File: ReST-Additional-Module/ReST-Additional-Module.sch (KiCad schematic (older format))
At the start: 15 parts, among them P1 02X10-MALE, P3 02-SCREW-TERM, P4 01X02-MALE, P5 02-SCREW-TERM, Q1 Q_BSH105

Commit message: Added Additional Module
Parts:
- removed C1: 10uF, ok-smd-generic:1206, symbol C
- removed P1: 02X10-MALE, Pin_Headers:Pin_Header_Angled_2x10, symbol CONN_02X10
- removed P4: 01X02-MALE, Pin_Headers:Pin_Header_Straight_1x02, symbol CONN_01X02
- removed P?: CONN_02X06, symbol CONN_02X06
- removed Q?: Q_NMOS_GSD, symbol Q_NMOS_GSD
- removed R1: 4.7K, ok-smd-generic:1206, symbol R
- added P1: CONN_02X06, Pin_Headers:Pin_Header_Angled_2x06, symbol CONN_02X06
- added Q2: Q_AOT240L, TO_SOT_Packages_THT:TO-220_Neutral123_Vertical_LargePads, symbol Q_NMOS_GDS
- P2: renamed from P5; footprint 5mm-pitch-terminal:mkds_1,5-2 -> Pin_Headers:Pin_Header_Straight_1x02
- P3: footprint 2:mpt_0,5%2f2-2,54 -> 5mm-pitch-terminal:mkds_1,5-2
- renumbered R2 to R1, R3 to R2, R4 to R3, R5 to R4
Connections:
- net labels added: PWM-ADD
- net labels removed: PWM-HEATER, T1
- wire segments 84 -> 40
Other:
- note removed: "Heater Thermistor"
- moved on the sheet: D1, D2, P2, Q1, R1, R2, R3, R4

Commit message: Saving
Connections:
- net +12V: now also P1.10 (P10), P1.12 (P12); no longer P1.2 (P2), P1.4 (P4)
- net +3V3: now also P1.4 (P4); no longer P1.10 (P10)
- net +5V: now also P1.1 (P1); no longer P1.9 (P9)
- net GND: now also P1.9 (P9); no longer P1.1 (P1), P1.3 (P3)
- net PWM-ADD: now also P1.3 (P3); no longer P1.12 (P12)
- no-connect marks 0 -> 1
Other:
- moved on the sheet: P1
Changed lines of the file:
@@
 L +5V #PWR02
 U 1 1 56A6A1BB
-P 2950 2900
-F 0 "#PWR02" H 2950 2750 50  0001 C CNN
-F 1 "+5V" H 2950 3040 50  0000 C CNN
-F 2 "" H 2950 2900 50  0000 C CNN
-F 3 "" H 2950 2900 50  0000 C CNN
-	1    2950 2900
-	0    -1   -1   0
+P 3050 3100
+F 0 "#PWR02" H 3050 2950 50  0001 C CNN
+F 1 "+5V" H 3050 3240 50  0000 C CNN
+F 2 "" H 3050 3100 50  0000 C CNN
+F 3 "" H 3050 3100 50  0000 C CNN
+	1    3050 3100
+	-1   0    0    1
 $EndComp
 $Comp
 L +3V3 #PWR03
 U 1 1 56A6A1DD
-P 3800 2900
-F 0 "#PWR03" H 3800 2750 50  0001 C CNN
-F 1 "+3V3" H 3800 3040 50  0000 C CNN
-F 2 "" H 3800 2900 50  0000 C CNN
-F 3 "" H 3800 2900 50  0000 C CNN
-	1    3800 2900
-	1    0    0    -1
+P 3750 2900
+F 0 "#PWR03" H 3750 2750 50  0001 C CNN
+F 1 "+3V3" H 3750 3040 50  0000 C CNN
+F 2 "" H 3750 2900 50  0000 C CNN
+F 3 "" H 3750 2900 50  0000 C CNN
+	1    3750 2900
+	0    1    1    0
 $EndComp
 $Comp
 L GND #PWR04
-U 1 1 56A6A1FF
-P 2950 3100
-F 0 "#PWR04" H 2950 2850 50  0001 C CNN
-F 1 "GND" H 2950 2950 50  0000 C CNN
-F 2 "" H 2950 3100 50  0000 C CNN
-F 3 "" H 2950 3100 50  0000 C CNN
-	1    2950 3100
-	1    0    0    -1
-$EndComp
-$Comp
-L GND #PWR05
 U 1 1 56A6B6EF
 P 6850 3850
-F 0 "#PWR05" H 6850 3600 50  0001 C CNN
+F 0 "#PWR04" H 6850 3600 50  0001 C CNN
 F 1 "GND" H 6850 3700 50  0000 C CNN
 F 2 "" H 6850 3850 50  0000 C CNN
@@
 $EndComp
 $Comp
-L +3V3 #PWR06
+L +3V3 #PWR05
 U 1 1 56A6D2B8
 P 5150 3250
-F 0 "#PWR06" H 5150 3100 50  0001 C CNN
+F 0 "#PWR05" H 5150 3100 50  0001 C CNN
 F 1 "+3V3" H 5150 3390 50  0000 C CNN
 F 2 "" H 5150 3250 50  0000 C CNN
@@
 $EndComp
 $Comp
-L +5V #PWR07
+L +5V #PWR06
 U 1 1 56A6D350
 P 5550 2750
-F 0 "#PWR07" H 5550 2600 50  0001 C CNN
+F 0 "#PWR06" H 5550 2600 50  0001 C CNN
 F 1 "+5V" H 5550 2890 50  0000 C CNN
 F 2 "" H 5550 2750 50  0000 C CNN
@@
 $EndComp
 $Comp
-L GND #PWR08
+L GND #PWR07
 U 1 1 56A6DF02
 P 5550 4050
-F 0 "#PWR08" H 5550 3800 50  0001 C CNN
+F 0 "#PWR07" H 5550 3800 50  0001 C CNN
 F 1 "GND" H 5550 3900 50  0000 C CNN
 F 2 "" H 5550 4050 50  0000 C CNN
@@
 Text Label 5050 3750 2    39   ~ 0
 PWM-ADD
-Text Label 3650 3000 0    39   ~ 0
+Text Label 3050 2900 2    39   ~ 0
 PWM-ADD
 $Comp
-L +12V #PWR09
+L +12V #PWR08
 U 1 1 56A7EB7B
 P 3300 3900
-F 0 "#PWR09" H 3300 3750 50  0001 C CNN
+F 0 "#PWR08" H 3300 3750 50  0001 C CNN
 F 1 "+12V" H 3300 4040 50  0000 C CNN
 F 2 "" H 3300 3900 50  0000 C CNN
@@
 $EndComp
 $Comp
-L GND #PWR010
+L GND #PWR09
 U 1 1 56A7EBB6
 P 2900 4000
-F 0 "#PWR010" H 2900 3750 50  0001 C CNN
+F 0 "#PWR09" H 2900 3750 50  0001 C CNN
 F 1 "GND" H 2900 3850 50  0000 C CNN
 F 2 "" H 2900 4000 50  0000 C CNN
@@
 $EndComp
 $Comp
-L +5V #PWR011
+L +5V #PWR010
 U 1 1 56A7EBF1
 P 3750 3900
-F 0 "#PWR011" H 3750 3750 50  0001 C CNN
+F 0 "#PWR010" H 3750 3750 50  0001 C CNN
 F 1 "+5V" H 3750 4040 50  0000 C CNN
 F 2 "" H 3750 3900 50  0000 C CNN
@@
 $EndComp
 $Comp
-L +3V3 #PWR012
+L +3V3 #PWR011
 U 1 1 56A7EC2C
 P 4200 3850
-F 0 "#PWR012" H 4200 3700 50  0001 C CNN
+F 0 "#PWR011" H 4200 3700 50  0001 C CNN
 F 1 "+3V3" H 4200 3990 50  0000 C CNN
 F 2 "" H 4200 3850 50  0000 C CNN
@@
 $EndComp
 $Comp
-L PWR_FLAG #FLG013
+L PWR_FLAG #FLG012
 U 1 1 56A7EC59
 P 4200 4000
-F 0 "#FLG013" H 4200 4095 50  0001 C CNN
+F 0 "#FLG012" H 4200 4095 50  0001 C CNN
 F 1 "PWR_FLAG" H 4200 4180 50  0000 C CNN
 F 2 "" H 4200 4000 50  0000 C CNN
@@
 $EndComp
 $Comp
-L PWR_FLAG #FLG014
+L PWR_FLAG #FLG013
 U 1 1 56A7EC9B
 P 3750 4000
-F 0 "#FLG014" H 3750 4095 50  0001 C CNN
+F 0 "#FLG013" H 3750 4095 50  0001 C CNN
 F 1 "PWR_FLAG" H 3750 4180 50  0000 C CNN
 F 2 "" H 3750 4000 50  0000 C CNN
@@
 $EndComp
 $Comp
-L PWR_FLAG #FLG015
+L PWR_FLAG #FLG014
 U 1 1 56A7ECD6
 P 3300 4000
-F 0 "#FLG015" H 3300 4095 50  0001 C CNN
+F 0 "#FLG014" H 3300 4095 50  0001 C CNN
 F 1 "PWR_FLAG" H 3300 4180 50  0000 C CNN
 F 2 "" H 3300 4000 50  0000 C CNN
@@
 $EndComp
 $Comp
-L PWR_FLAG #FLG016
+L PWR_FLAG #FLG015
 U 1 1 56A7ED11
 P 2900 3900
-F 0 "#FLG016" H 2900 3995 50  0001 C CNN
+F 0 "#FLG015" H 2900 3995 50  0001 C CNN
 F 1 "PWR_FLAG" H 2900 4080 50  0000 C CNN
 F 2 "" H 2900 3900 50  0000 C CNN
@@
 Power Definitions
 $Comp
-L +12V #PWR017
+L +12V #PWR016
 U 1 1 56AC08E7
-P 3650 2400
-F 0 "#PWR017" H 3650 2250 50  0001 C CNN
-F 1 "+12V" H 3650 2540 50  0000 C CNN
-F 2 "" H 3650 2400 50  0000 C CNN
-F 3 "" H 3650 2400 50  0000 C CNN
-	1    3650 2400
-	1    0    0    -1
-$EndComp
-$Comp
-L GND #PWR018
+P 3750 2400
+F 0 "#PWR016" H 3750 2250 50  0001 C CNN
+F 1 "+12V" H 3750 2540 50  0000 C CNN
+F 2 "" H 3750 2400 50  0000 C CNN
+F 3 "" H 3750 2400 50  0000 C CNN
+	1    3750 2400
+	1    0    0    -1
+$EndComp
+$Comp
+L GND #PWR017
 U 1 1 56AC091C
-P 2950 2400
-F 0 "#PWR018" H 2950 2150 50  0001 C CNN
-F 1 "GND" H 2950 2250 50  0000 C CNN
-F 2 "" H 2950 2400 50  0000 C CNN
-F 3 "" H 2950 2400 50  0000 C CNN
-	1    2950 2400
+P 3050 2400
+F 0 "#PWR017" H 3050 2150 50  0001 C CNN
+F 1 "GND" H 3050 2250 50  0000 C CNN
+F 2 "" H 3050 2400 50  0000 C CNN
+F 3 "" H 3050 2400 50  0000 C CNN
+	1    3050 2400
 	-1   0    0    1
 $EndComp
@@
 L CONN_02X06 P1
 U 1 1 56AD3C5B
-P 3300 2750
-F 0 "P1" H 3300 3100 50  0000 C CNN
-F 1 "CONN_02X06" H 3300 2400 50  0000 C CNN
-F 2 "Pin_Headers:Pin_Header_Angled_2x06" H 3300 1550 50  0001 C CNN
-F 3 "" H 3300 1550 50  0000 C CNN
-	1    3300 2750
-	1    0    0    -1
-$EndComp
-Wire Wire Line
-	3650 2400 3650 2800
-Wire Wire Line
-	3650 2500 3550 2500
-Wire Wire Line
-	3650 2600 3550 2600
-Connection ~ 3650 2500
-Wire Wire Line
-	3650 2700 3550 2700
-Connection ~ 3650 2600
-Wire Wire Line
-	3650 2800 3550 2800
-Connection ~ 3650 2700
-Wire Wire Line
-	2950 2400 2950 2800
-Wire Wire Line
-	2950 2500 3050 2500
-Wire Wire Line
-	2950 2600 3050 2600
-Connection ~ 2950 2500
-Wire Wire Line
-	2950 2700 3050 2700
-Connection ~ 2950 2600
-Wire Wire Line
-	2950 2800 3050 2800
-Connection ~ 2950 2700
-Wire Wire Line
-	2950 2900 3050 2900
-Wire Wire Line
-	3550 2900 3800 2900
-Wire Wire Line
-	3050 3000 2950 3000
-Wire Wire Line
-	2950 3000 2950 3100
-Wire Wire Line
-	3650 3000 3550 3000
+P 3400 2750
+F 0 "P1" H 3400 3100 50  0000 C CNN
+F 1 "CONN_02X06" H 3400 2400 50  0000 C CNN
+F 2 "Pin_Headers:Pin_Header_Angled_2x06" H 3400 1550 50  0001 C CNN
+F 3 "" H 3400 1550 50  0000 C CNN
+	1    3400 2750
+	1    0    0    1
+$EndComp
+Wire Wire Line
+	3750 2400 3750 2800
+Wire Wire Line
+	3750 2500 3650 2500
+Wire Wire Line
+	3750 2600 3650 2600
+Connection ~ 3750 2500
+Wire Wire Line
+	3750 2700 3650 2700
+Connection ~ 3750 2600
+Wire Wire Line
+	3750 2800 3650 2800
+Connection ~ 3750 2700
+Wire Wire Line
+	3050 2400 3050 2800
+Wire Wire Line
+	3050 2500 3150 2500
+Wire Wire Line
+	3050 2600 3150 2600
+Connection ~ 3050 2500
+Wire Wire Line
+	3050 2700 3150 2700
+Connection ~ 3050 2600
+Wire Wire Line
+	3050 2800 3150 2800
+Connection ~ 3050 2700
 Wire Notes Line
 	2650 2100 4050 2100
@@
 Wire Notes Line
 	4050 3400 4050 2100
+Wire Wire Line
+	3750 2900 3650 2900
+Wire Wire Line
+	3150 2900 3050 2900
+Wire Wire Line
+	3050 3100 3050 3000
+Wire Wire Line
+	3050 3000 3150 3000
+NoConn ~ 3650 3000
 $EndSCHEMATC

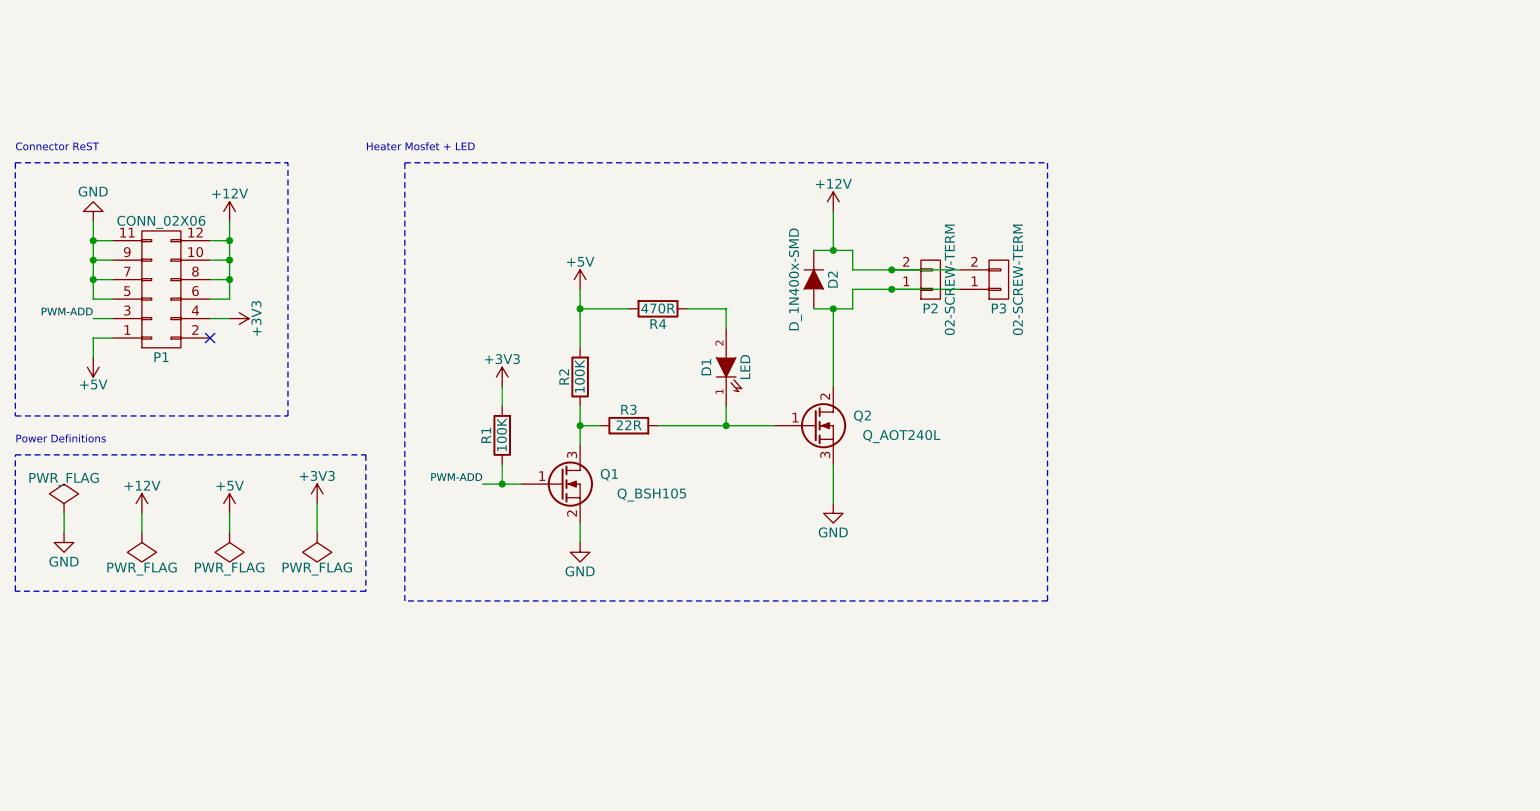
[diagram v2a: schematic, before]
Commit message: Changed Additional-Board and Pinout
Sooo... I thought adding multiple Additional Module Boards would be bit much. Looked back at some older projects of mine and thought that using something like the uln2803 would be pretty neat (like 8 NPN Transitors, each 500mah and that in a DIL-18 Package IIRC) Which turns price really down, aswell as the size of the module. 
But using that one resultet in removing many extra pinouts, leaving with only 5 unused pins which will be broken out extra. This may change when the lcd pinout is finished. adding extra pinout for the additional board could also work out (as it occupies 8 pwm pins). I will look to copy that all into the schematic

Also missing: I2C EEPROM/Flash for settings
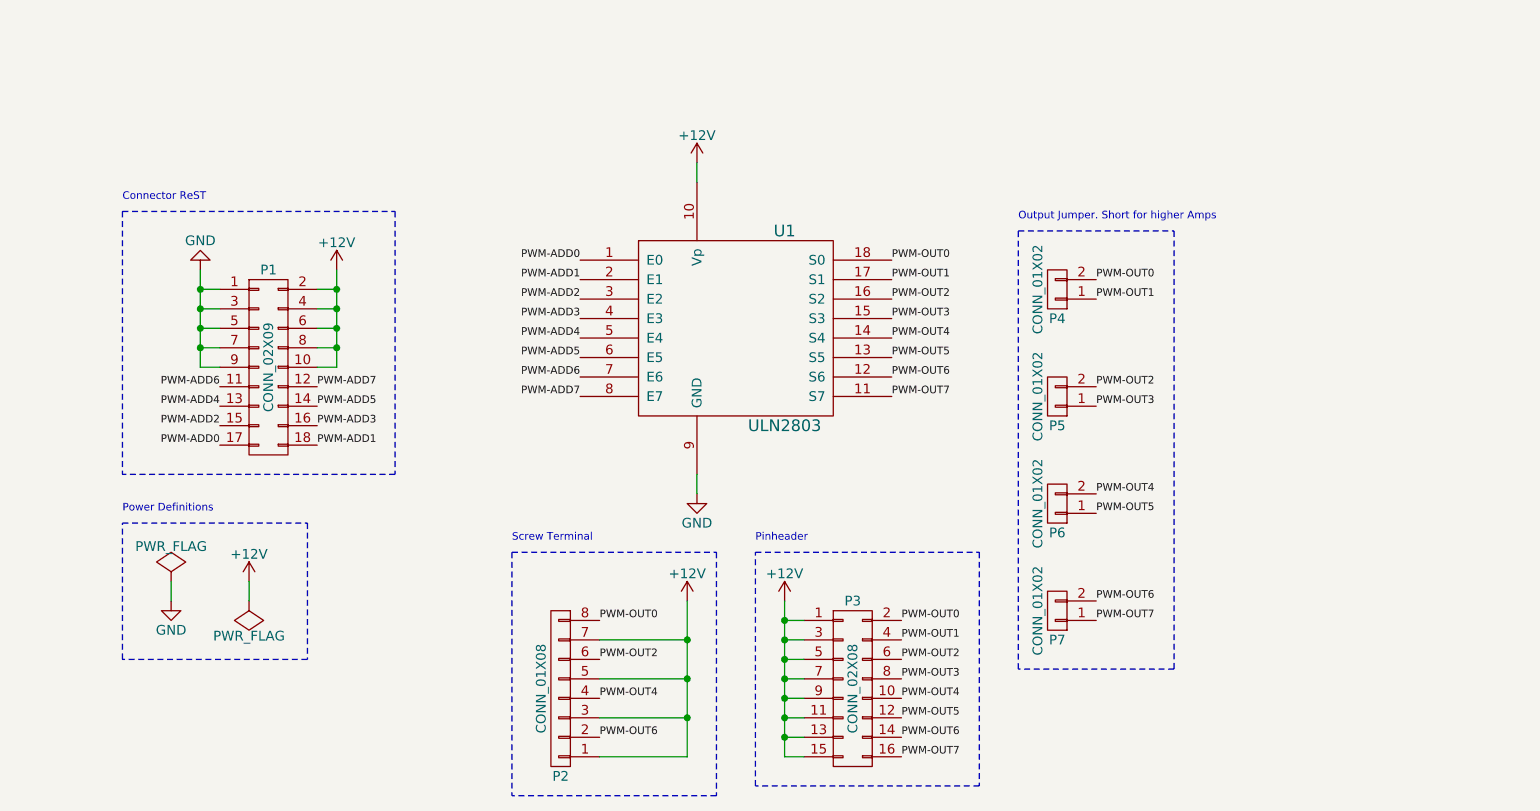
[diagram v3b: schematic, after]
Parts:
- removed D1: LED, LEDs:LED_1206, symbol LED
- removed D2: D_1N400x-SMD, DO-214AC(SMA):DO-214AC(SMA), symbol D
- removed P1: CONN_02X06, Pin_Headers:Pin_Header_Angled_2x06, symbol CONN_02X06
- removed P2: 02-SCREW-TERM, Pin_Headers:Pin_Header_Straight_1x02, symbol CONN_01X02
- removed P3: 02-SCREW-TERM, 5mm-pitch-terminal:mkds_1,5-2, symbol CONN_01X02
- removed Q1: Q_BSH105, TO_SOT_Packages_SMD:SOT-23, symbol Q_NMOS_GSD
- removed Q2: Q_AOT240L, TO_SOT_Packages_THT:TO-220_Neutral123_Vertical_LargePads, symbol Q_NMOS_GDS
- removed R1, R2: 100K, ok-smd-generic:1206, symbol R
- removed R3: 22R, ok-smd-generic:1206, symbol R
- removed R4: 470R, ok-smd-generic:1206, symbol R
- added P1: CONN_02X09, Pin_Headers:Pin_Header_Angled_2x09, symbol CONN_02X09
- added P2: CONN_01X08, 2:mpt_0,5%2f8-2,54, symbol CONN_01X08
- added P3: CONN_02X08, Pin_Headers:Pin_Header_Straight_2x08, symbol CONN_02X08
- added P4, P5, P6, P7: CONN_01X02, Pin_Headers:Pin_Header_Straight_1x02, symbol CONN_01X02
- added U1: ULN2803, Housings_DIP:DIP-18_W7.62mm_LongPads, symbol ULN2803
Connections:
- net +12V: now also P1.10 (P10), P1.2 (P2), P1.4 (P4), P1.6 (P6), P1.8 (P8), P2.1 (P1), P2.3 (P3), P2.5 (P5), P2.7 (P7), P3.1 (P1), P3.11 (P11), P3.13 (P13), P3.15 (P15), P3.3 (P3), P3.5 (P5), P3.7 (P7), P3.9 (P9), U1.10 (Vp)
- net GND: now also P1.1 (P1), P1.3 (P3), P1.5 (P5), P1.7 (P7), P1.9 (P9), U1.9 (GND)
- new net PWM-ADD0: P1.17 (P17), U1.1 (E0)
- new net PWM-ADD1: P1.18 (P18), U1.2 (E1)
- new net PWM-ADD2: P1.15 (P15), U1.3 (E2)
- new net PWM-ADD3: P1.16 (P16), U1.4 (E3)
- new net PWM-ADD4: P1.13 (P13), U1.5 (E4)
- new net PWM-ADD5: P1.14 (P14), U1.6 (E5)
- new net PWM-ADD6: P1.11 (P11), U1.7 (E6)
- new net PWM-ADD7: P1.12 (P12), U1.8 (E7)
- new net PWM-OUT0: P2.8 (P8), P3.2 (P2), P4.2 (P2), U1.18 (S0)
- new net PWM-OUT1: P3.4 (P4), P4.1 (P1), U1.17 (S1)
- new net PWM-OUT2: P2.6 (P6), P3.6 (P6), P5.2 (P2), U1.16 (S2)
- new net PWM-OUT3: P3.8 (P8), P5.1 (P1), U1.15 (S3)
- new net PWM-OUT4: P2.4 (P4), P3.10 (P10), P6.2 (P2), U1.14 (S4)
- new net PWM-OUT5: P3.12 (P12), P6.1 (P1), U1.13 (S5)
- new net PWM-OUT6: P2.2 (P2), P3.14 (P14), P7.2 (P2), U1.12 (S6)
- new net PWM-OUT7: P3.16 (P16), P7.1 (P1), U1.11 (S7)
- no-connect marks 1 -> 0
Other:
- note added: "Output Jumper. Short for higher Amps"
- note added: "Pinheader"
- note added: "Screw Terminal"
- note removed: "Heater Mosfet + LED\n"
